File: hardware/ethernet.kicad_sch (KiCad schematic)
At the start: 90 parts, among them J5 USB_C_Receptacle, Q1 BSS138, Q2 BSS138, U11 TXS0202YZPR, U14 KSZ9031RNXCA, U4 CCGM1A1, X1 ECS-2520MV-250-xx

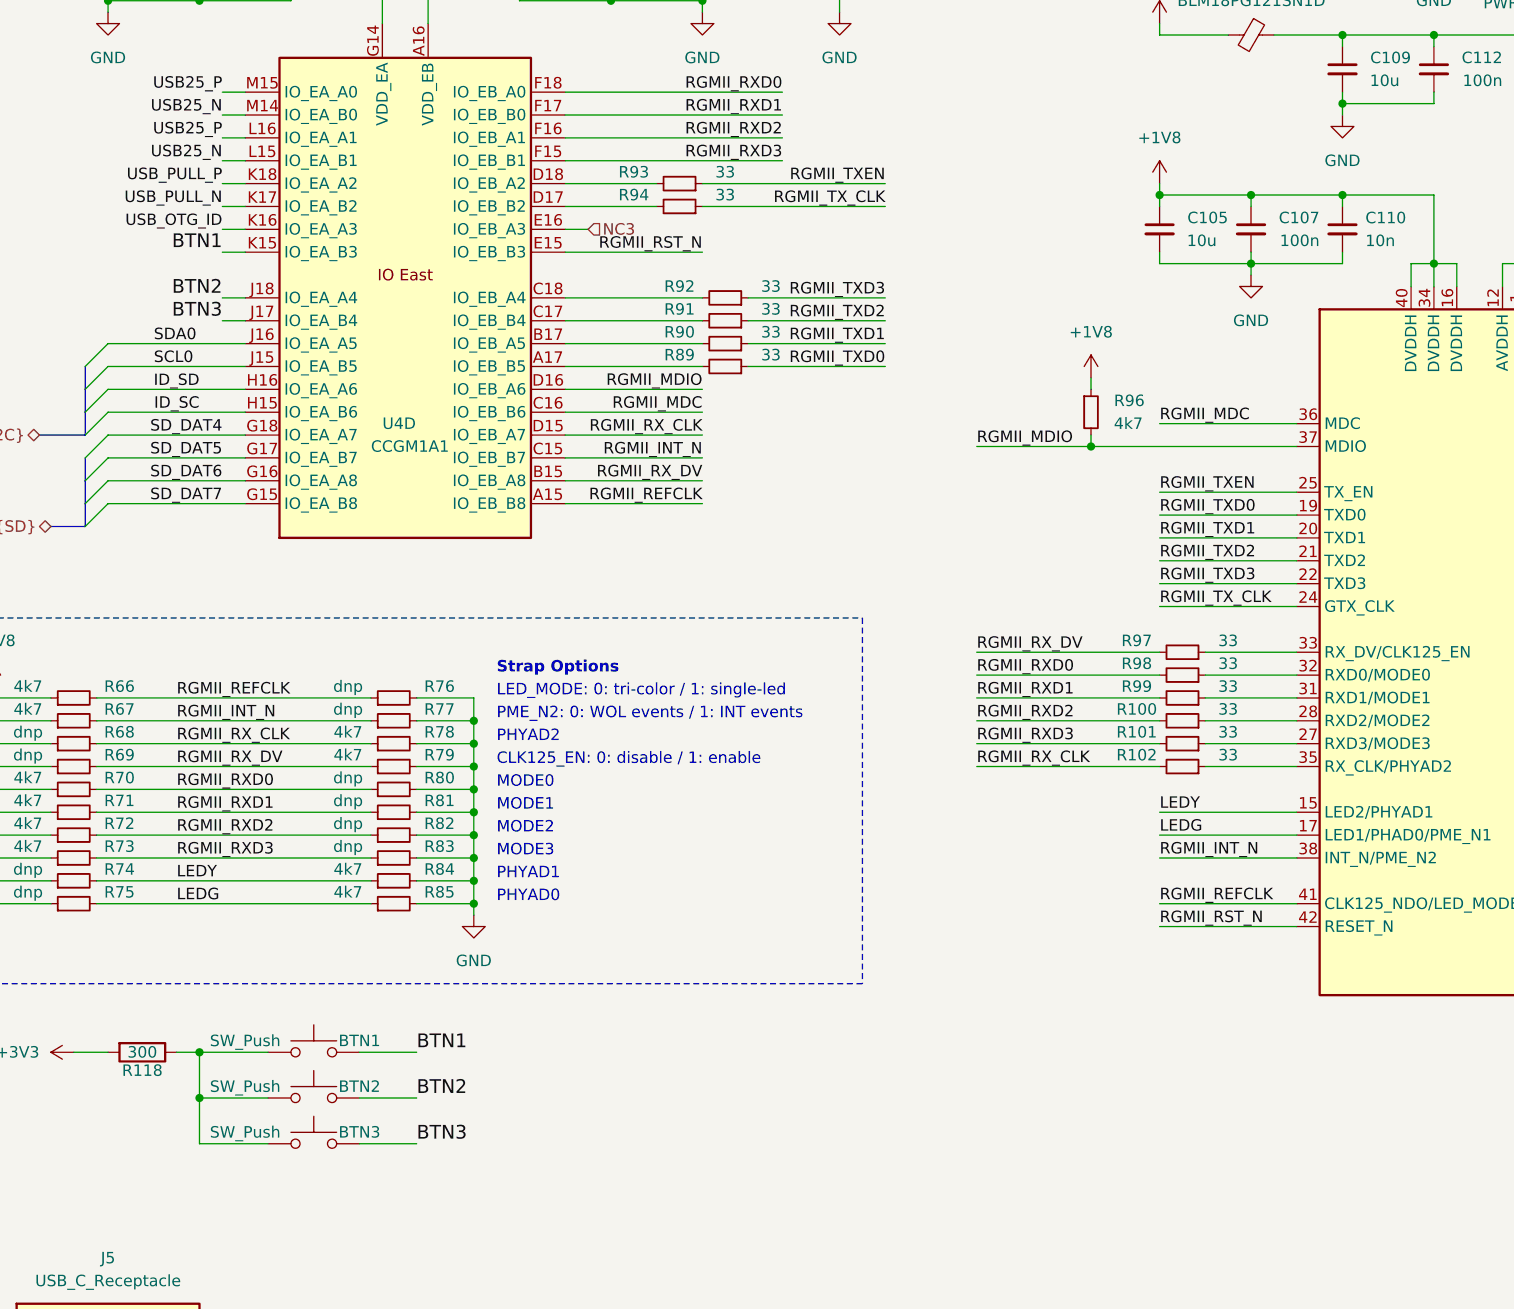
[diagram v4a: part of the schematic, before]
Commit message: GPIO are now routed differential
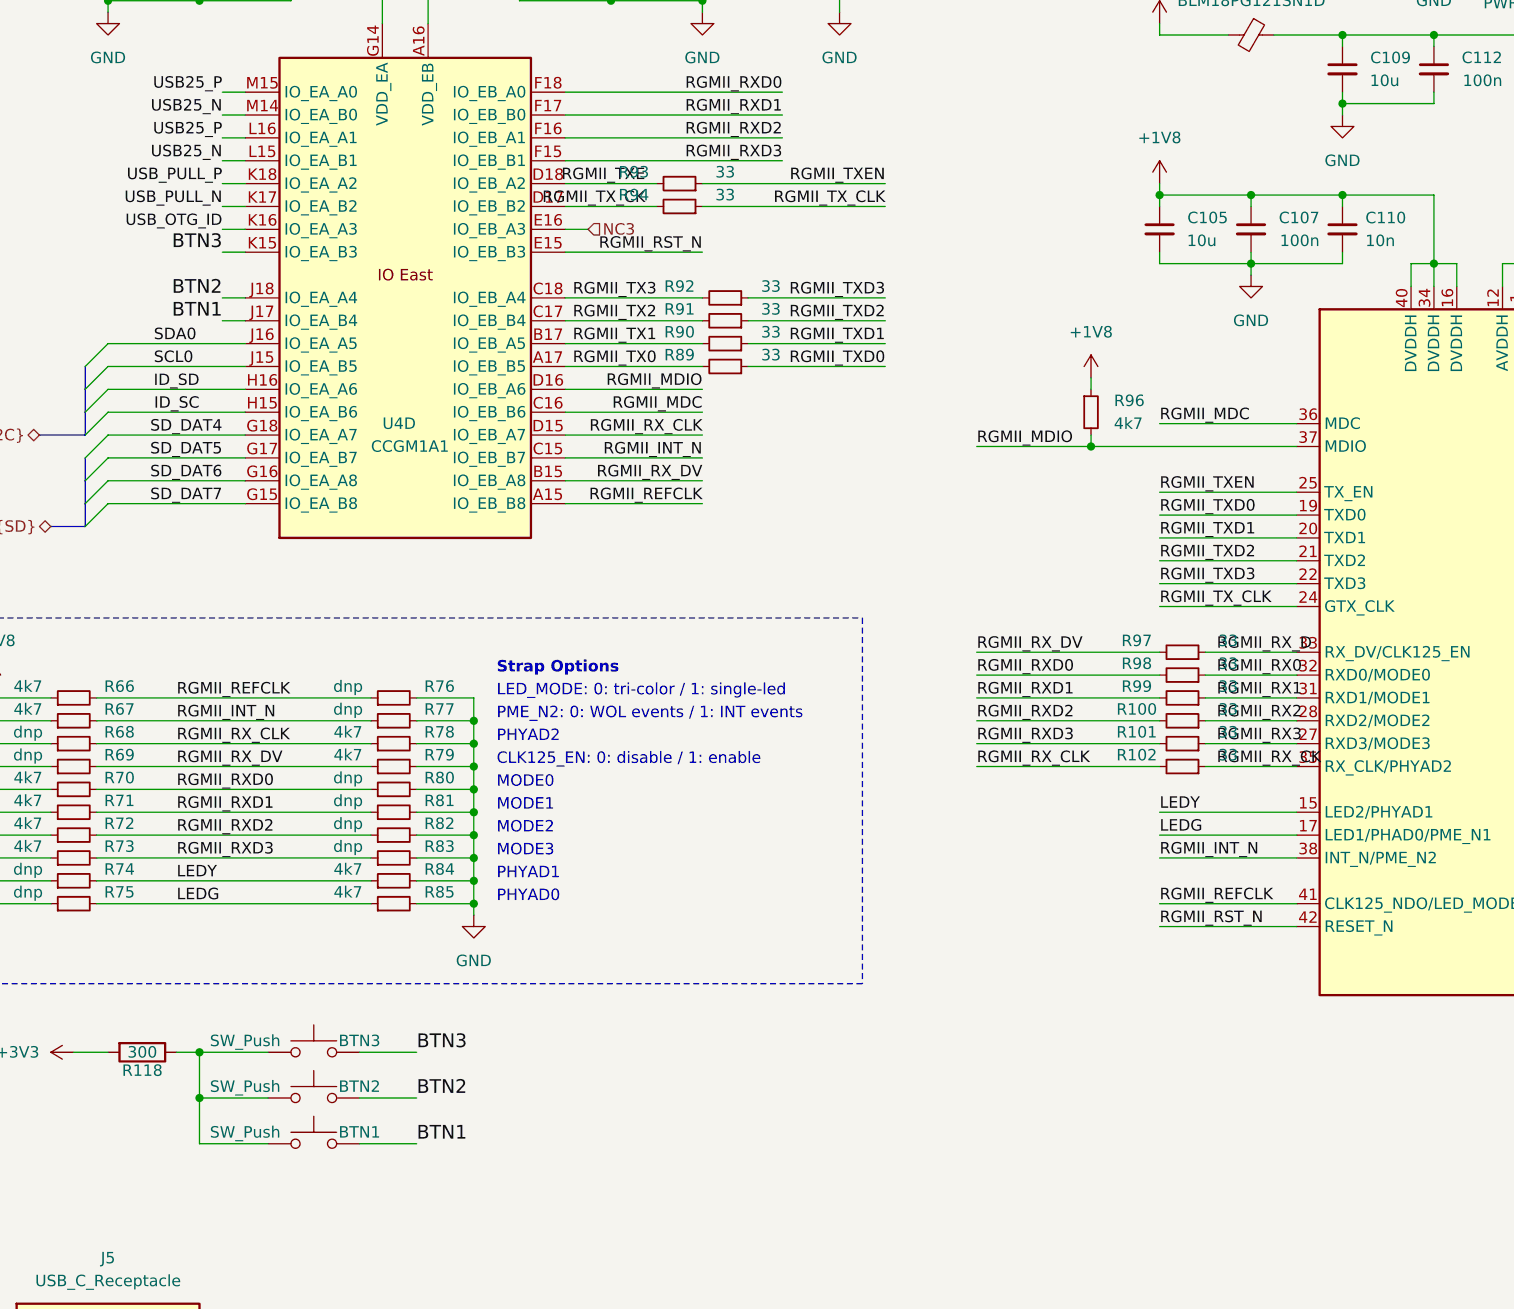
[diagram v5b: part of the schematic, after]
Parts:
- renumbered BTN3 to BTN1, BTN1 to BTN3
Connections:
- net BTN1: now also BTN1.2, U4.J17 (IO_EA_B4); no longer BTN3.2, U4.K15 (IO_EA_B3)
- net BTN3: now also BTN3.2, U4.K15 (IO_EA_B3); no longer BTN1.2, U4.J17 (IO_EA_B4)
- net RGMII_TXE: now reaches R93.2, U4.D18 (IO_EB_A2)
- net RGMII_RX1: now reaches R99.1, U14.31 (RXD1/MODE1)
- net RGMII_RX0: now reaches R98.1, U14.32 (RXD0/MODE0)
- net RGMII_TX0: now reaches R89.2, U4.A17 (IO_EB_B5)
- net RGMII_TX1: now reaches R90.2, U4.B17 (IO_EB_A5)
- net RGMII_TX2: now reaches R91.2, U4.C17 (IO_EB_B4)
- net RGMII_TX3: now reaches R92.2, U4.C18 (IO_EB_A4)
- net RGMII_TX_CK: now reaches R94.2, U4.D17 (IO_EB_B2)
- net RGMII_RX3: now reaches R101.1, U14.27 (RXD3/MODE3)
- net RGMII_RX2: now reaches R100.1, U14.28 (RXD2/MODE2)
- net RGMII_RX_D: now reaches R97.1, U14.33 (RX_DV/CLK125_EN)
- net RGMII_RX_CK: now reaches R102.1, U14.35 (RX_CLK/PHYAD2)
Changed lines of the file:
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@@
+		)
+	)
+	(label "RGMII_RX_CK"
+		(at 163.83 119.38 0)
+		(effects
+			(font
+				(size 1.27 1.27)
+			)
+			(justify left bottom)
 		)
 	)
@@
 		)
 	)
+	(label "RGMII_RX0"
+		(at 163.83 109.22 0)
+		(effects
+			(font
+				(size 1.27 1.27)
+			)
+			(justify left bottom)
+		)
+	)
 	(label "ID_SC"
 		(at 50.8 80.01 180)
@@
 		)
 	)
+	(label "RGMII_TX_CK"
+		(at 100.33 57.15 180)
+		(effects
+			(font
+				(size 1.27 1.27)
+			)
+			(justify right bottom)
+		)
+	)
 	(label "RGMII_RXD1"
 		(at 115.57 46.99 180)
@@
 		)
 	)
+	(label "RGMII_RX2"
+		(at 163.83 114.3 0)
+		(effects
+			(font
+				(size 1.27 1.27)
+			)
+			(justify left bottom)
+		)
+	)
+	(label "RGMII_TX3"
+		(at 101.6 67.31 180)
+		(effects
+			(font
+				(size 1.27 1.27)
+			)
+			(justify right bottom)
+		)
+	)
 	(label "ETH3_N"
 		(at 248.92 101.6 180)
@@
 		)
 	)
+	(label "RGMII_TX0"
+		(at 101.6 74.93 180)
+		(effects
+			(font
+				(size 1.27 1.27)
+			)
+			(justify right bottom)
+		)
+	)
 	(label "SD_DAT4"
 		(at 53.34 82.55 180)
@@
 		)
 	)
-	(label "BTN3"
+	(label "BTN1"
 		(at 53.34 69.85 180)
 		(effects
@@
 			)
 			(justify right bottom)
+		)
+	)
+	(label "RGMII_RX1"
+		(at 163.83 111.76 0)
+		(effects
+			(font
+				(size 1.27 1.27)
+			)
+			(justify left bottom)
 		)
 	)
@@
 		)
 	)
+	(label "RGMII_TX2"
+		(at 101.6 69.85 180)
+		(effects
+			(font
+				(size 1.27 1.27)
+			)
+			(justify right bottom)
+		)
+	)
 	(label "RGMII_RXD0"
 		(at 137.16 109.22 0)
@@
 		)
 	)
+	(label "RGMII_RX3"
+		(at 163.83 116.84 0)
+		(effects
+			(font
+				(size 1.27 1.27)
+			)
+			(justify left bottom)
+		)
+	)
 	(label "BTN2"
 		(at 74.93 156.21 0)
@@
 		)
 	)
+	(label "RGMII_TXE"
+		(at 100.33 54.61 180)
+		(effects
+			(font
+				(size 1.27 1.27)
+			)
+			(justify right bottom)
+		)
+	)
 	(label "RGMII_MDC"
 		(at 106.68 80.01 180)
@@
 		)
 	)
-	(label "BTN3"
+	(label "BTN1"
 		(at 74.93 161.29 0)
 		(effects
@@
 		)
 	)
+	(label "RGMII_RX_D"
+		(at 163.83 106.68 0)
+		(effects
+			(font
+				(size 1.27 1.27)
+			)
+			(justify left bottom)
+		)
+	)
 	(label "SD_DAT6"
 		(at 53.34 87.63 180)
@@
 		)
 	)
-	(label "BTN1"
+	(label "BTN3"
 		(at 74.93 151.13 0)
 		(effects
@@
 		)
 	)
-	(label "BTN1"
+	(label "BTN3"
 		(at 53.34 62.23 180)
 		(effects
@@
 	(label "USB_PULL_N"
 		(at 119.38 219.71 180)
+		(effects
+			(font
+				(size 1.27 1.27)
+			)
+			(justify right bottom)
+		)
+	)
+	(label "RGMII_TX1"
+		(at 101.6 72.39 180)
 		(effects
 			(font
@@
 		(on_board yes)
 		(dnp no)
-		(property "Reference" "BTN1"
+		(property "Reference" "BTN3"
 			(at 68.58 149.86 0)
 			(effects
@@
 			(project "ulx5m-gs"
 				(path "/9e5cbfd6-8186-4817-919e-acd256336bc8/5c4580e2-a442-496c-941e-38ded55dcc84"
-					(reference "BTN1")
+					(reference "BTN3")
 					(unit 1)
 				)
@@
 		(on_board yes)
 		(dnp no)
-		(property "Reference" "BTN3"
+		(property "Reference" "BTN1"
 			(at 68.58 160.02 0)
 			(effects
@@
 			(project "ulx5m-gs"
 				(path "/9e5cbfd6-8186-4817-919e-acd256336bc8/5c4580e2-a442-496c-941e-38ded55dcc84"
-					(reference "BTN3")
+					(reference "BTN1")
 					(unit 1)
 				)

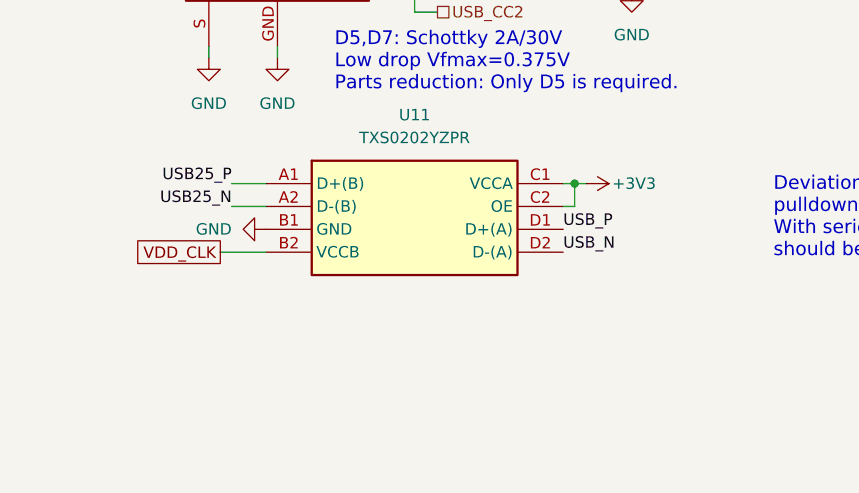
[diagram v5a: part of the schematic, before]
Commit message: Switching A and B on TXS0202YZPR adding pass resistors
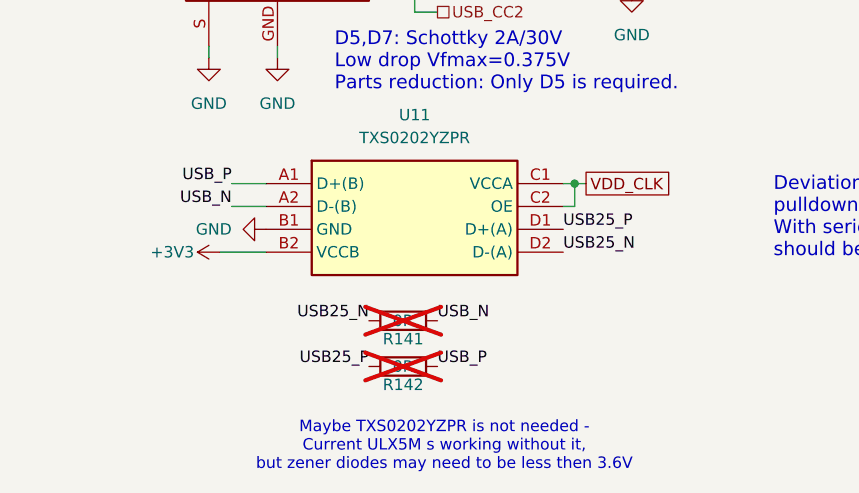
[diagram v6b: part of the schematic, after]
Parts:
- added R141, R142: 0R, Resistor_SMD:R_0402_1005Metric, symbol Device:R
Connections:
- net +3V3: now also U11.B2 (VCCB); no longer U11.C1 (VCCA), U11.C2 (OE)
- net USB25_N: now also U11.D2 (D-(A)), R141.1; no longer U11.A2 (D-(B))
- net USB25_P: now also U11.D1 (D+(A)), R142.1; no longer U11.A1 (D+(B))
- net USB_N: now also U11.A2 (D-(B)), R141.2; no longer U11.D2 (D-(A))
- net USB_P: now also U11.A1 (D+(B)), R142.2; no longer U11.D1 (D+(A))
- net VDD_CLK: now also U11.C1 (VCCA), U11.C2 (OE); no longer U11.B2 (VCCB)
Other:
- note added: "Maybe TXS0202YZPR is not needed - Current ULX5M s working without it, but zener diodes may need to be less then 3.6V"
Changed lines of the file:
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@@
 		)
 	)
+	(text "Maybe TXS0202YZPR is not needed - \nCurrent ULX5M s working without it, \nbut zener diodes may need to be less then 3.6V"
+		(exclude_from_sim no)
+		(at 59.182 255.27 0)
+		(effects
+			(font
+				(size 1.27 1.27)
+			)
+		)
+	)
 	(text "D+ 1.5k pullp for \nfull speed device\nmode USB1.1"
 		(exclude_from_sim no)
@@
 	)
 	(label "USB_P"
-		(at 72.39 231.14 0)
+		(at 35.56 226.06 180)
 		(effects
 			(font
 				(size 1.27 1.27)
 			)
-			(justify left bottom)
+			(justify right bottom)
 		)
 	)
@@
 	)
 	(label "USB25_P"
-		(at 35.56 226.06 180)
+		(at 72.39 231.14 0)
 		(effects
 			(font
 				(size 1.27 1.27)
 			)
-			(justify right bottom)
+			(justify left bottom)
 		)
 	)
@@
 	)
 	(label "USB_N"
-		(at 72.39 233.68 0)
+		(at 35.56 228.6 180)
 		(effects
 			(font
 				(size 1.27 1.27)
 			)
-			(justify left bottom)
+			(justify right bottom)
+		)
+	)
+	(label "USB25_N"
+		(at 50.8 241.3 180)
+		(effects
+			(font
+				(size 1.27 1.27)
+			)
+			(justify right bottom)
 		)
 	)
@@
 		)
 	)
+	(label "USB25_P"
+		(at 50.8 246.38 180)
+		(effects
+			(font
+				(size 1.27 1.27)
+			)
+			(justify right bottom)
+		)
+	)
 	(label "RGMII_INT_N"
 		(at 106.68 85.09 180)
@@
 		)
 	)
+	(label "USB_P"
+		(at 58.42 246.38 0)
+		(effects
+			(font
+				(size 1.27 1.27)
+			)
+			(justify left bottom)
+		)
+	)
 	(label "ETH2_P"
 		(at 248.92 111.76 180)
@@
 		)
 	)
+	(label "USB_N"
+		(at 58.42 241.3 0)
+		(effects
+			(font
+				(size 1.27 1.27)
+			)
+			(justify left bottom)
+		)
+	)
 	(label "BTN1"
 		(at 74.93 161.29 0)
@@
 	)
 	(label "USB25_N"
-		(at 35.56 228.6 180)
+		(at 72.39 233.68 0)
 		(effects
 			(font
 				(size 1.27 1.27)
 			)
-			(justify right bottom)
+			(justify left bottom)
 		)
 	)
@@
 	(global_label "VDD_CLK"
 		(shape passive)
-		(at 34.29 233.68 180)
+		(at 74.93 226.06 0)
 		(fields_autoplaced yes)
 		(effects
@@
 				(size 1.27 1.27)
 			)
-			(justify right)
+			(justify left)
 		)
 		(property "Intersheetrefs" "${INTERSHEET_REFS}"
-			(at 24.2518 233.68 0)
+			(at 84.9682 226.06 0)
 			(effects
 				(font
 					(size 1.27 1.27)
 				)
-				(justify right)
+				(justify left)
 				(hide yes)
 			)
@@
 	)
 	(symbol
+		(lib_id "Device:R")
+		(at 54.61 246.38 90)
+		(mirror x)
+		(unit 1)
+		(exclude_from_sim no)
+		(in_bom yes)
+		(on_board yes)
+		(dnp yes)
+		(property "Reference" "R142"
+			(at 54.61 248.412 90)
+			(effects
+				(font
+					(size 1.27 1.27)
+				)
+			)
+		)
+		(property "Value" "0R"
+			(at 54.61 246.38 90)
+			(effects
+				(font
+					(size 1.27 1.27)
+				)
+			)
+		)
+		(property "Footprint" "Resistor_SMD:R_0402_1005Metric"
+			(at 54.61 244.602 90)
+			(effects
+				(font
+					(size 1.27 1.27)
+				)
+				(hide yes)
+			)
+		)
+		(property "Datasheet" ""
+			(at 54.61 246.38 0)
+			(effects
+				(font
+					(size 1.27 1.27)
+				)
+			)
+		)
+		(property "Description" ""
+			(at 54.61 246.38 0)
+			(effects
+				(font
+					(size 1.27 1.27)
+				)
+				(hide yes)
+			)
+		)
+		(pin "1"
+		)
+		(pin "2"
+		)
+		(instances
+			(project "ulx5m-gs"
+				(path "/9e5cbfd6-8186-4817-919e-acd256336bc8/5c4580e2-a442-496c-941e-38ded55dcc84"
+					(reference "R142")
+					(unit 1)
+				)
+			)
+		)
+	)
+	(symbol
 		(lib_id "Device:C_Small")
 		(at 157.48 59.69 0)
@@
 	)
 	(symbol
+		(lib_id "Device:R")
+		(at 54.61 241.3 90)
+		(mirror x)
+		(unit 1)
+		(exclude_from_sim no)
+		(in_bom yes)
+		(on_board yes)
+		(dnp yes)
+		(property "Reference" "R141"
+			(at 54.61 243.332 90)
+			(effects
+				(font
+					(size 1.27 1.27)
+				)
+			)
+		)
+		(property "Value" "0R"
+			(at 54.61 241.3 90)
+			(effects
+				(font
+					(size 1.27 1.27)
+				)
+			)
+		)
+		(property "Footprint" "Resistor_SMD:R_0402_1005Metric"
+			(at 54.61 239.522 90)
+			(effects
+				(font
+					(size 1.27 1.27)
+				)
+				(hide yes)
+			)
+		)
+		(property "Datasheet" ""
+			(at 54.61 241.3 0)
+			(effects
+				(font
+					(size 1.27 1.27)
+				)
+			)
+		)
+		(property "Description" ""
+			(at 54.61 241.3 0)
+			(effects
+				(font
+					(size 1.27 1.27)
+				)
+				(hide yes)
+			)
+		)
+		(pin "1"
+		)
+		(pin "2"
+		)
+		(instances
+			(project "ulx5m-gs"
+				(path "/9e5cbfd6-8186-4817-919e-acd256336bc8/5c4580e2-a442-496c-941e-38ded55dcc84"
+					(reference "R141")
+					(unit 1)
+				)
+			)
+		)
+	)
+	(symbol
 		(lib_id "Device:R_Small")
 		(at 109.22 72.39 270)
@@
 		(lib_name "+5V_1")
 		(lib_id "power:+5V")
-		(at 74.93 226.06 270)
+		(at 34.29 233.68 90)
 		(unit 1)
 		(exclude_from_sim no)
@@
 		(dnp no)
 		(property "Reference" "#PWR0176"
-			(at 71.12 226.06 0)
+			(at 38.1 233.68 0)
 			(effects
 				(font
@@
 		)
 		(property "Value" "+3V3"
-			(at 80.264 226.06 90)
+			(at 28.956 233.68 90)
 			(effects
 				(font
@@
 		)
 		(property "Footprint" ""
-			(at 74.93 226.06 0)
+			(at 34.29 233.68 0)
 			(effects
 				(font
@@
 		)
 		(property "Datasheet" ""
-			(at 74.93 226.06 0)
+			(at 34.29 233.68 0)
 			(effects
 				(font
@@
 		)
 		(property "Description" "Power symbol creates a global label with name \"+5V\""
-			(at 74.93 226.06 0)
+			(at 34.29 233.68 0)
 			(effects
 				(font
